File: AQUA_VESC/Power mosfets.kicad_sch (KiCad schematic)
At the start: 53 parts, among them Q1 TK3R2E06PL, Q2 TK3R2E06PL, Q3 TK3R2E06PL, Q4 TK3R2E06PL, Q5 TK3R2E06PL, Q6 TK3R2E06PL

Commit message: AQUA VESC仮完成
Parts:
- removed C50, C57: 330u, 63V, specific_footprint_library:CP_10x20mm_hor_with_model_mirrored, symbol Device:C_Polarized
- added NT4, NT5, NT6, NT7, NT8, NT9: NetTie_2, NetTie:NetTie-2_SMD_Pad0.5mm, symbol Device:NetTie_2
- renumbered C51 to C50, C52 to C51, C53 to C52, C54 to C53, C55 to C54, C56 to C55, C58 to C56, C59 to C57, C60 to C58, C61 to C59, R39 to R38, R40 to R39, R41 to R40, R42 to R41, R43 to R42, R44 to R43, R45 to R44, R46 to R45, R47 to R46, R48 to R47, R49 to R48, R50 to R49, R51 to R50, R52 to R51, R53 to R52, R54 to R53, R55 to R54, R56 to R55, R57 to R56, R58 to R57, R59 to R58, R60 to R59, R61 to R60, R62 to R61, R63 to R62, R64 to R63, R65 to R64, R66 to R65, R67 to R66, R68 to R67, R69 to R68
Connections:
- net GNDPWR: now also NT5.2, NT7.2, NT9.2
- net H1_LOW: now also NT4.1; no longer C48.2, Q2.3 (S), R42.2, R44.2, R45.2
- net H2_LOW: now also NT6.1; no longer C53.2, Q4.3 (S), R52.2, R54.2, R55.2
- net H3_LOW: now also NT8.1; no longer C57.2, Q6.3 (S), R62.2, R64.2, R66.2
- new net: C48.2, NT4.2, Q2.3 (S), R42.2, R44.2, R45.2
- new net: C57.2, NT8.2, Q6.3 (S), R62.2, R64.2, R66.2
- new net: C53.2, NT6.2, Q4.3 (S), R52.2, R54.2, R55.2
- new net SPA: NT5.1
- new net SPB: NT7.1
- new net SPC: NT9.1

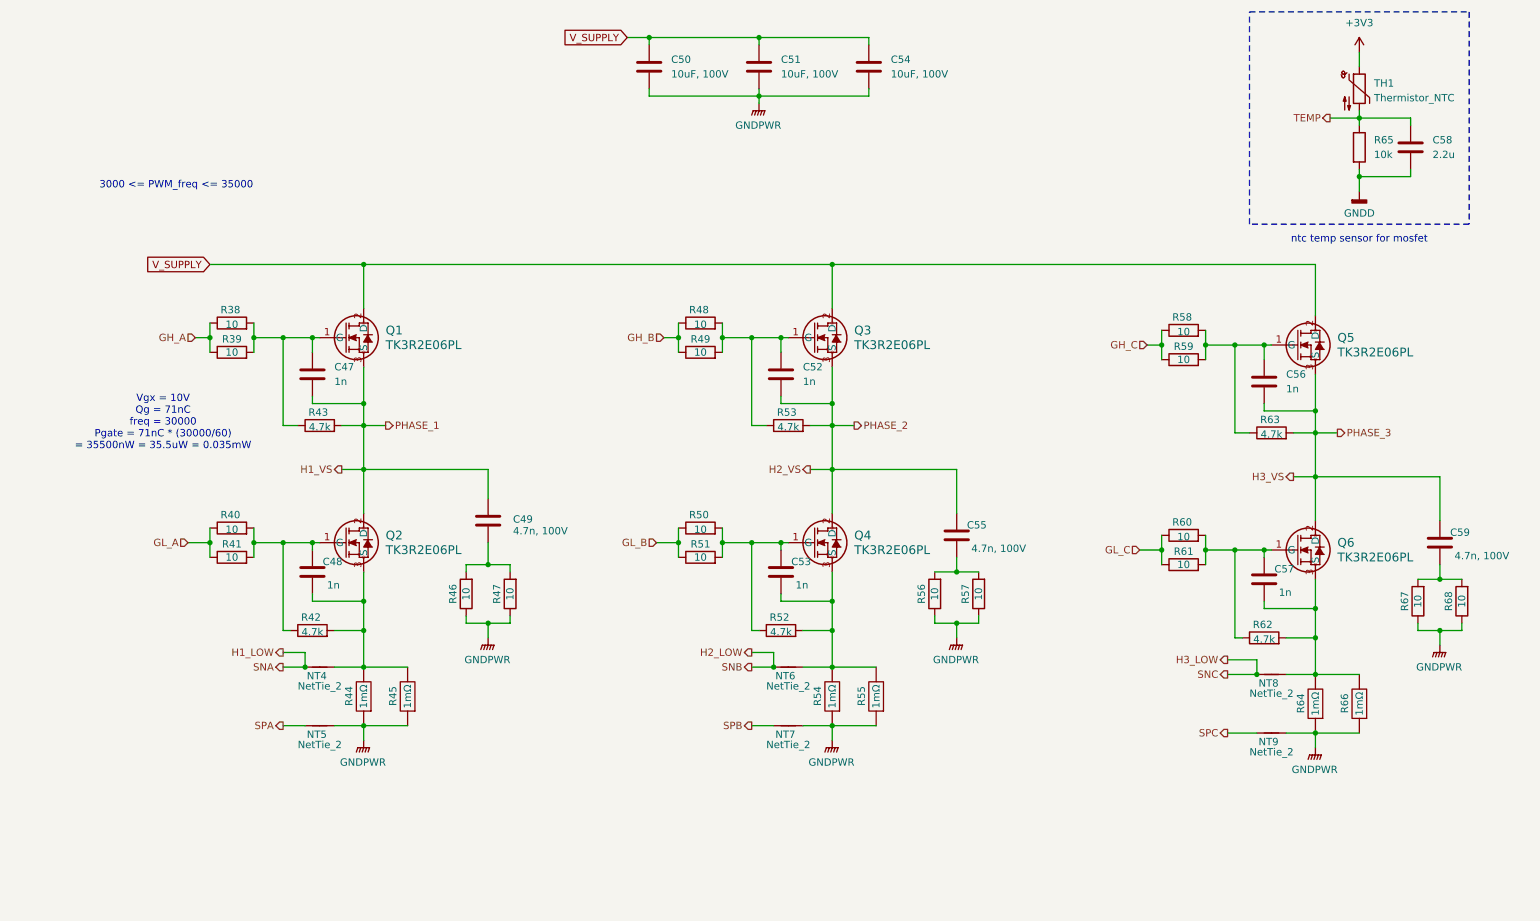
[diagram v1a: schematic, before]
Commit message: AQUA_VESC REV01作成
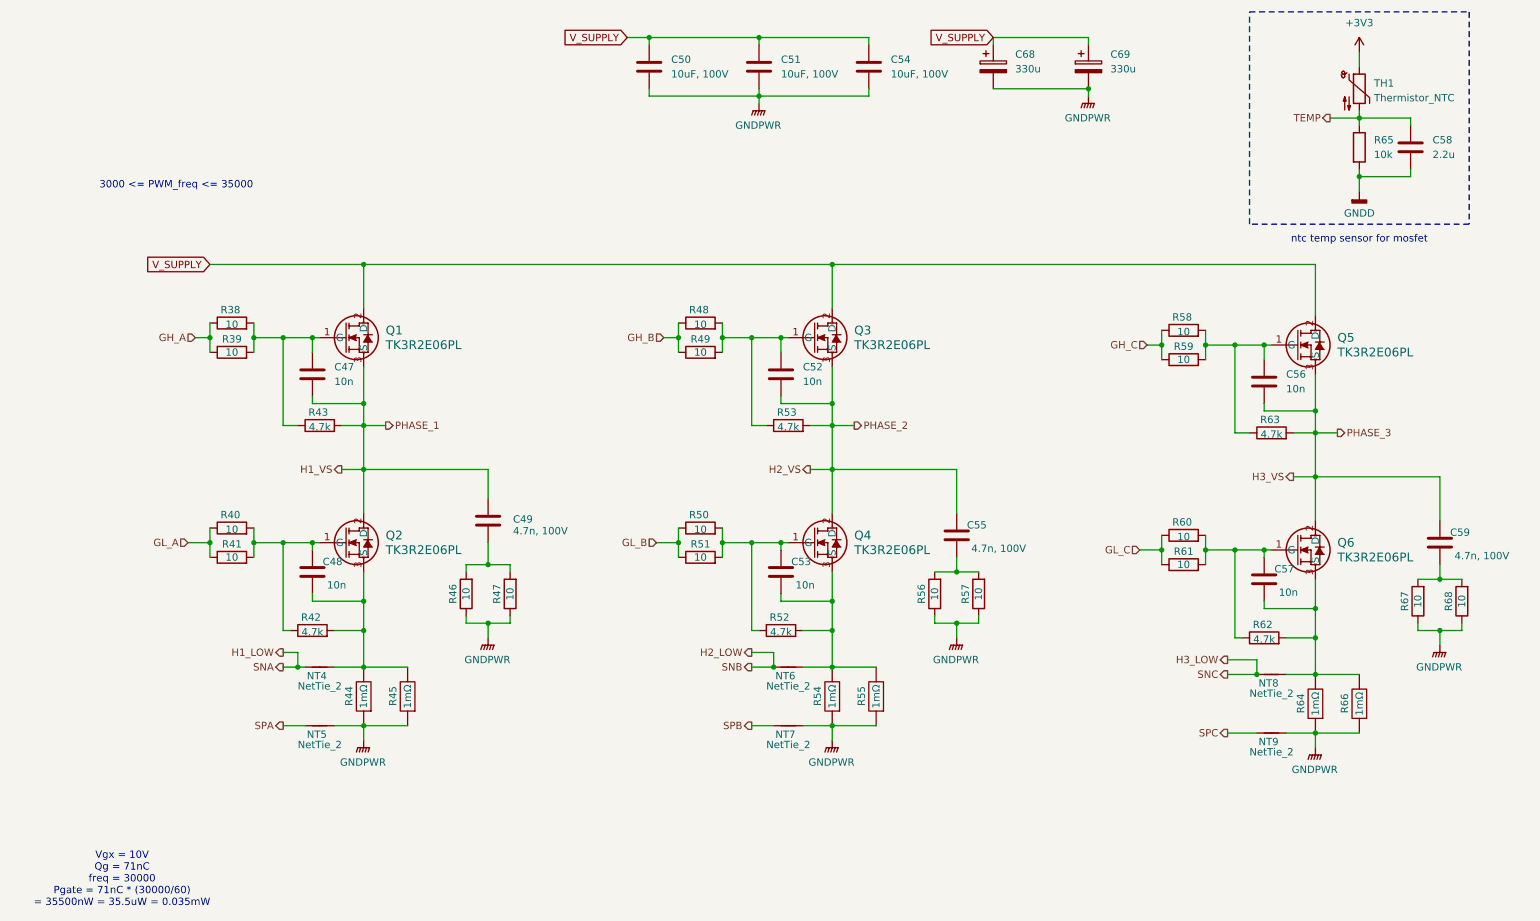
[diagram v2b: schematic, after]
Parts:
- added C68, C69: 330u, Capacitor_THT:CP_Radial_D10.0mm_P5.00mm, symbol Device:C_Polarized
- C47, C48, C52, C53, C56, C57: value 1n -> 10n
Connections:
- net GNDPWR: now also C68.2, C69.2
- net V_SUPPLY: now also C68.1, C69.1

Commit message: 制御基板REV01完成
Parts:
- renumbered C68 to C56, C69 to C57, C56 to C58, C57 to C59, C58 to C60, C59 to C61, R38 to R37, R39 to R38, R40 to R39, R41 to R40, R42 to R41, R43 to R42, R44 to R43, R45 to R44, R46 to R45, R47 to R46, R48 to R47, R49 to R48, R50 to R49, R51 to R50, R52 to R51, R53 to R52, R54 to R53, R55 to R54, R56 to R55, R57 to R56, R58 to R57, R59 to R58, R60 to R59, R61 to R60, R62 to R61, R63 to R62, R64 to R63, R65 to R64, R66 to R65, R67 to R66, R68 to R67

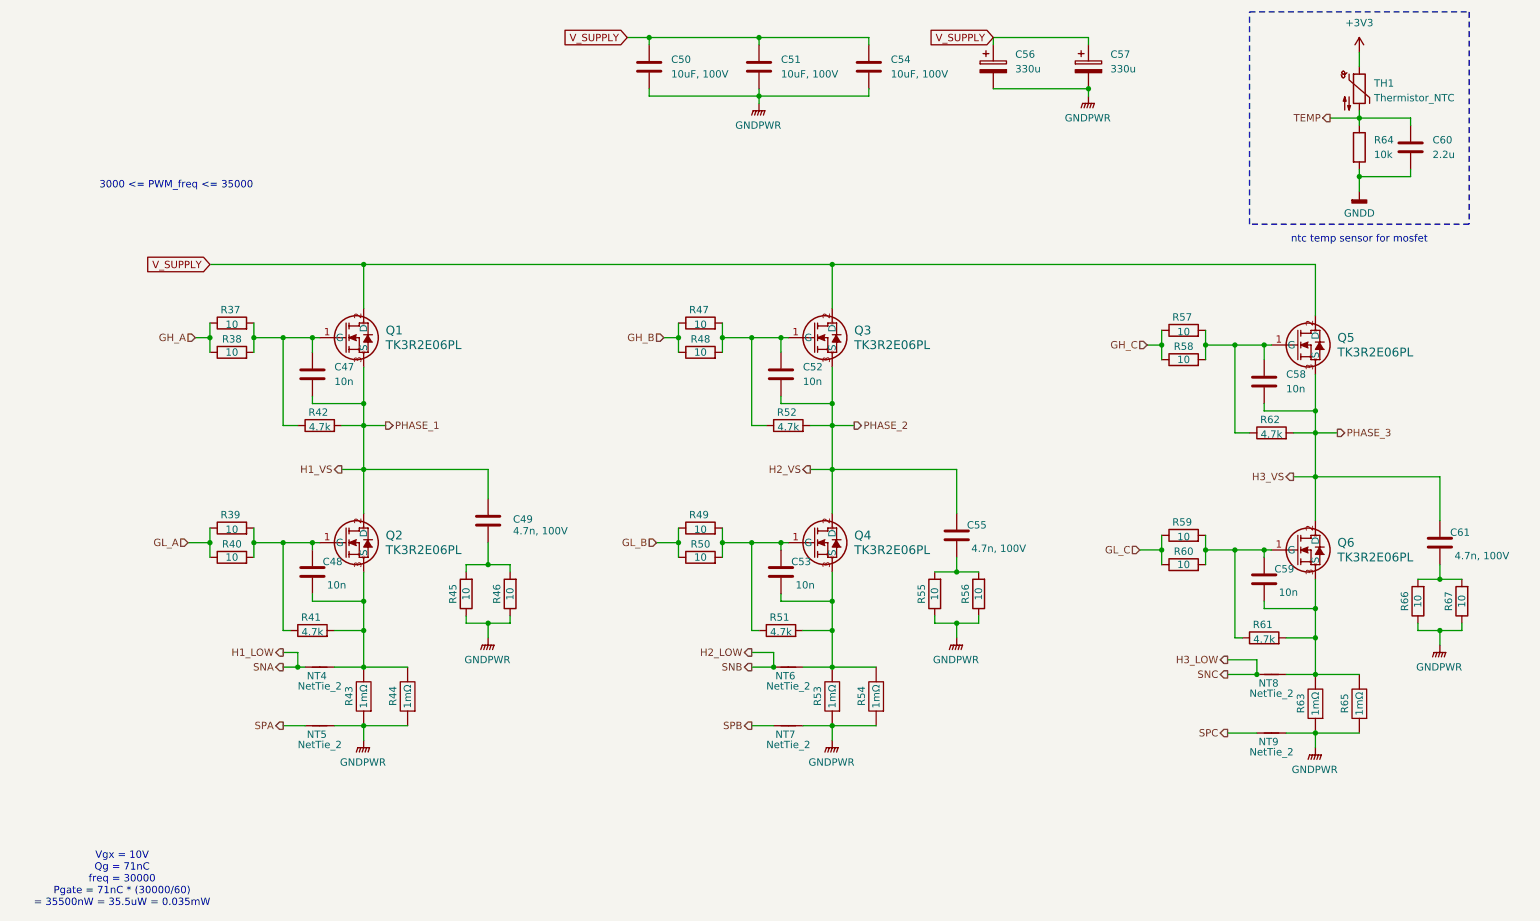
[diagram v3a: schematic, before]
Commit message: 方針変更、back_connector_escにMT60を使用しないことに
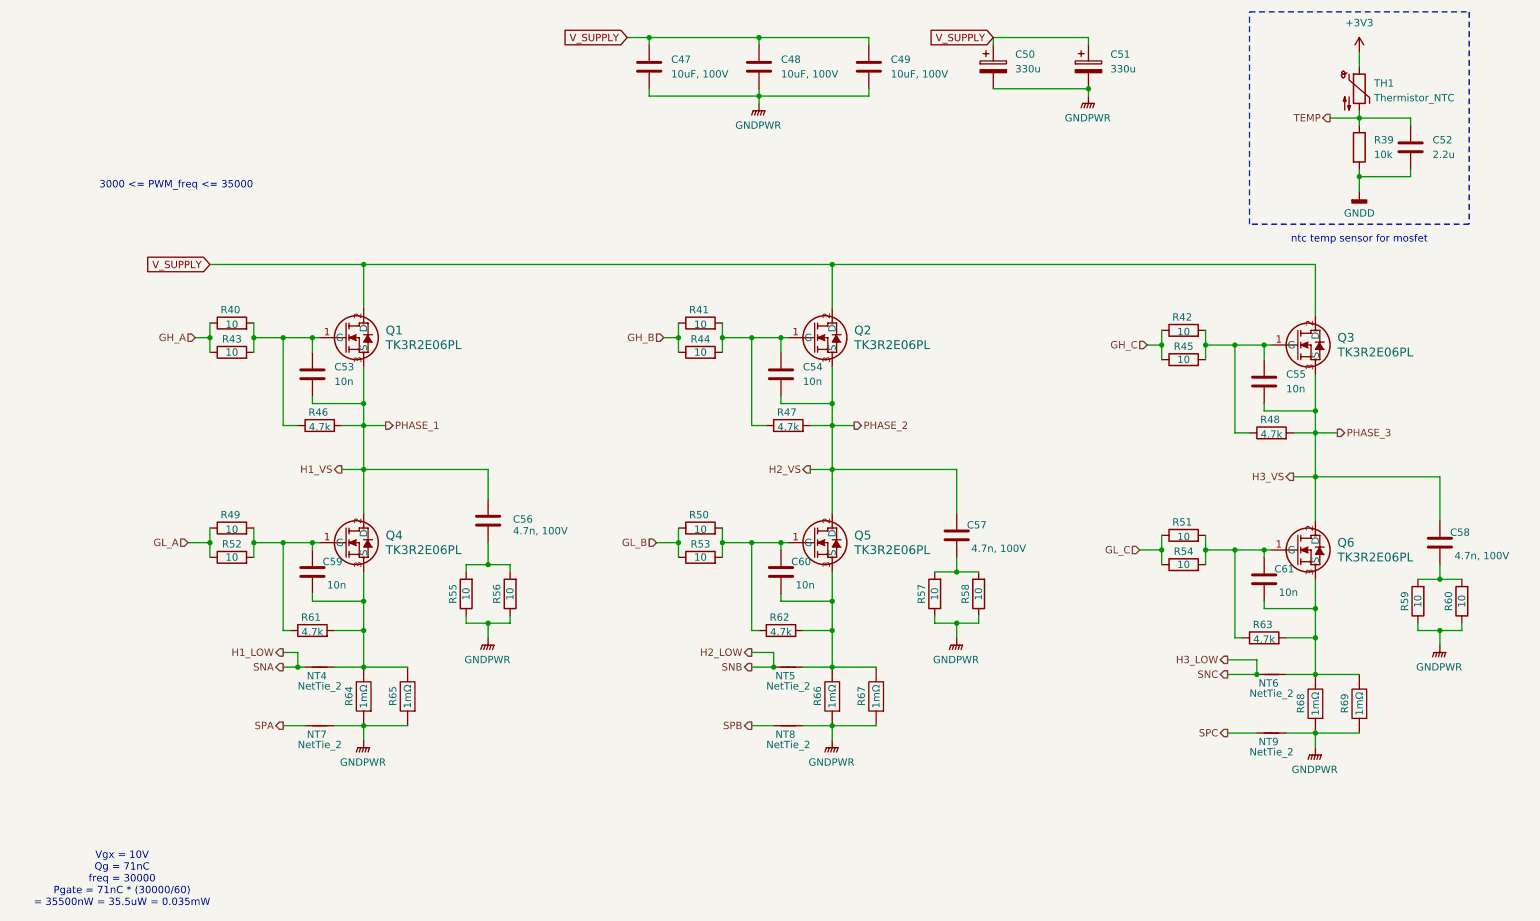
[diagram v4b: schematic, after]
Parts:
- renumbered C50 to C47, C51 to C48, C54 to C49, C56 to C50, C57 to C51, C60 to C52, C47 to C53, C52 to C54, C58 to C55, C49 to C56, C55 to C57, C61 to C58, C48 to C59, C53 to C60, C59 to C61, NT6 to NT5, NT8 to NT6, NT5 to NT7, NT7 to NT8, Q3 to Q2, Q5 to Q3, Q2 to Q4, Q4 to Q5, R64 to R39, R37 to R40, R47 to R41, R57 to R42, R38 to R43, R48 to R44, R58 to R45, R42 to R46, R52 to R47, R62 to R48, R39 to R49, R49 to R50, R59 to R51, R40 to R52, R50 to R53, R60 to R54, R45 to R55, R46 to R56, R55 to R57, R56 to R58, R66 to R59, R67 to R60, R41 to R61, R51 to R62, R61 to R63, R43 to R64, R44 to R65, R53 to R66, R54 to R67, R63 to R68, R65 to R69

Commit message: ESC周りの配線用基板進捗
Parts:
- C50, C51: footprint Capacitor_THT:CP_Radial_D10.0mm_P5.00mm -> specific_footprint_library:CP_Radial_D10.0mm_P5.00mm_nofill
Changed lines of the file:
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@@
 			)
 		)
-		(property "Footprint" "Capacitor_THT:CP_Radial_D10.0mm_P5.00mm"
+		(property "Footprint" "specific_footprint_library:CP_Radial_D10.0mm_P5.00mm_nofill"
 			(at 178.7652 36.83 0)
 			(effects
@@
 			)
 		)
-		(property "Footprint" "Capacitor_THT:CP_Radial_D10.0mm_P5.00mm"
+		(property "Footprint" "specific_footprint_library:CP_Radial_D10.0mm_P5.00mm_nofill"
 			(at 195.2752 36.83 0)
 			(effects
